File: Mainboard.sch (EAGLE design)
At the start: 15 parts, among them IC1 LM358N, IC2 LM358N, IC3 LM358N, Q1 IRF530, Q2 IRF530

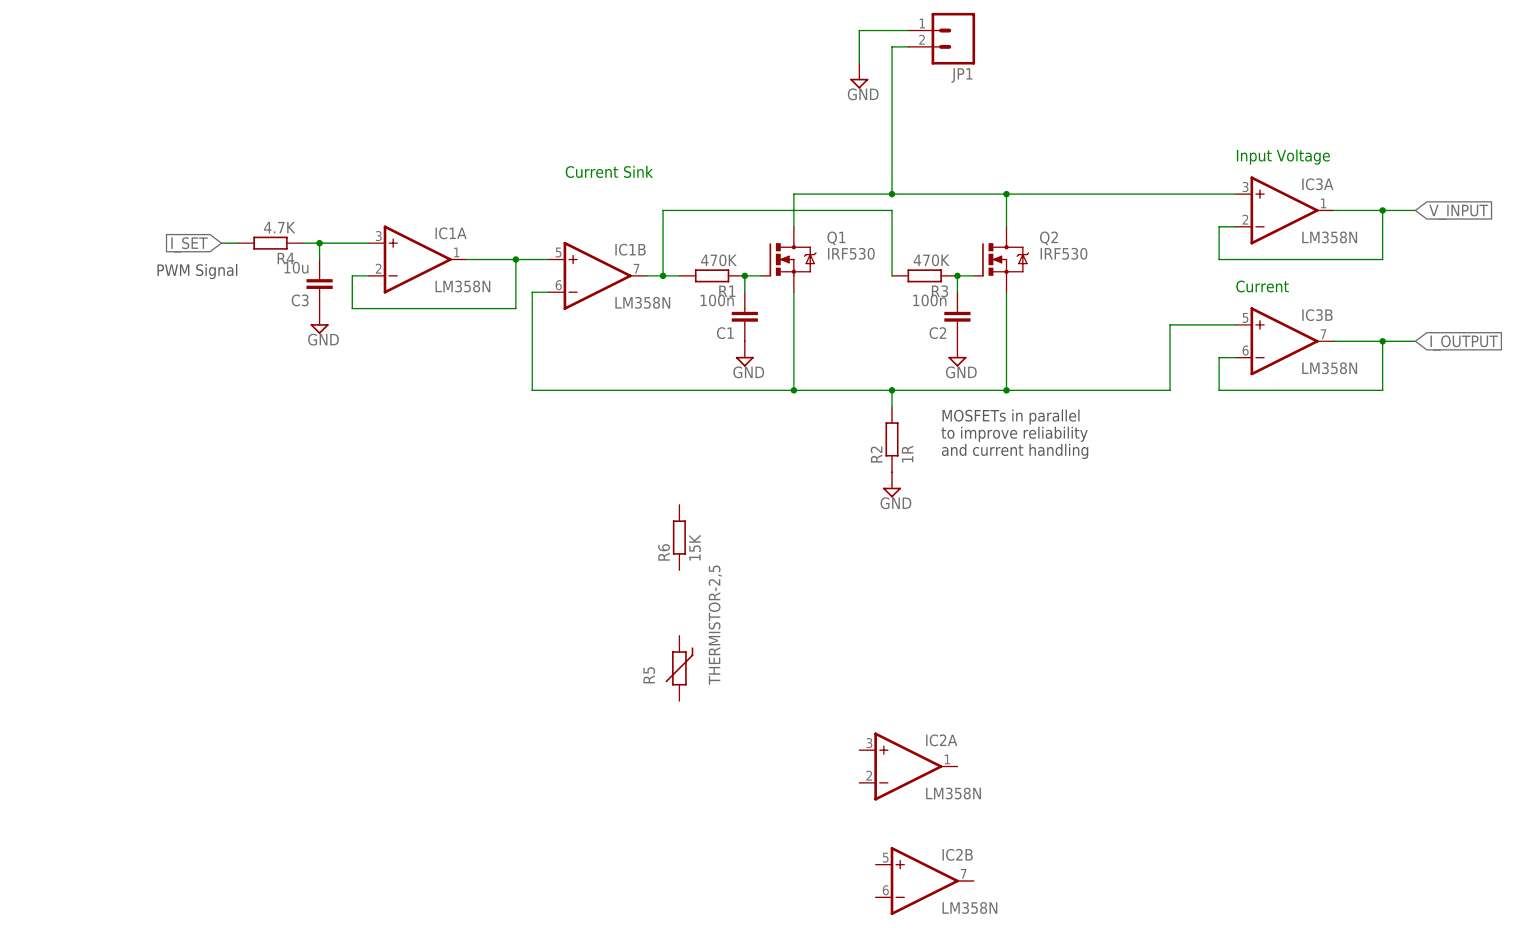
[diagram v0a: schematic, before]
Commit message: Tweak to PWM filters
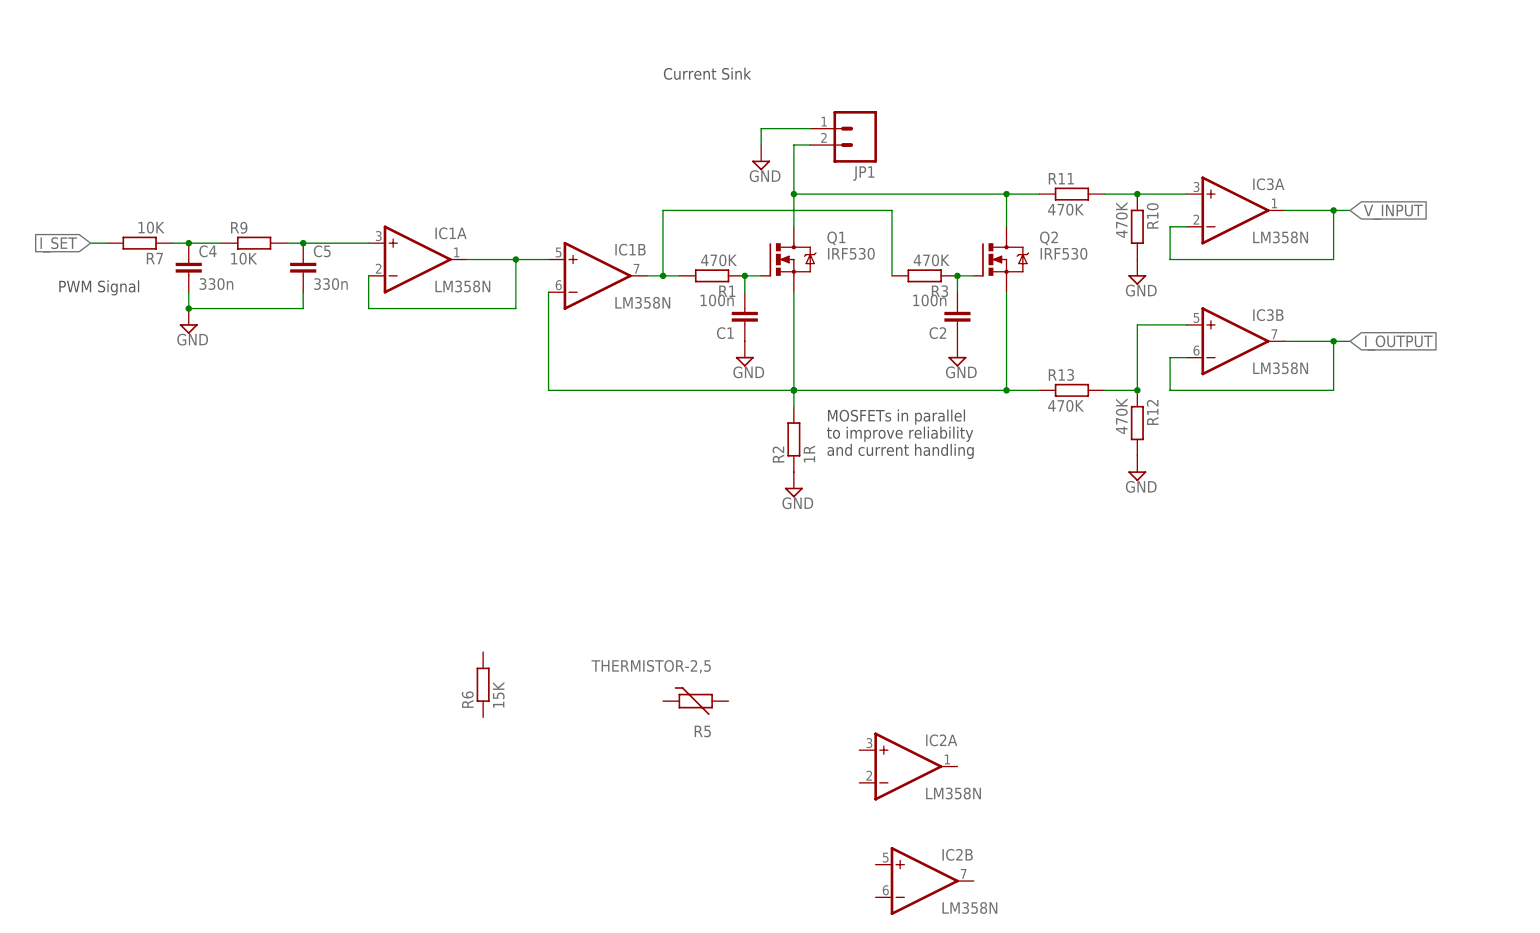
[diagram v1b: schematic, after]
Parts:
- removed C3: 10u, rcl:C-EU025-025X050
- removed R4: 4.7K, rcl:R-EU_0204/7
- added C4, C5: 330n, rcl:C-EU025-025X050
- added R10, R11, R12, R13: 470K, rcl:R-EU_0204/7
- added R7, R9: 10K, rcl:R-EU_0204/7
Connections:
- removed net I_SET: R4.2
- removed net N$7: C3.2, IC1A.+IN, R4.1
- new net N$11: IC3A.+IN, R10.1, R11.2
- new net N$12: IC3B.+IN, R12.1, R13.2
- new net N$8: C5.1, R9.2
- new net N$9: C4.1, R7.1, R9.1
- net GND: now also C4.2, C5.2, R10.2, R12.2; no longer C3.1
- net N$4: now also R13.1; no longer IC3B.+IN
- net N$5: now also R11.1; no longer IC3A.+IN
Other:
- note removed: "Current"
- note removed: "Input Voltage"
- moved on the sheet: IC3A, IC3B, JP1, R2, R5, R6
